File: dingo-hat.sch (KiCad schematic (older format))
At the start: 53 parts, among them J1 LiPo-Power, J10 PJ-037B, J11 Bypass-Power, J12 Chassis-Out, J13 i2c_display, J14 NEOPIXEL, J15 MPU-9250, J2 Raspberry_Pi_2_3, J24 3mm_Mount, J25 3mm_Mount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

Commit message: updated footprints to handsolder
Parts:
- C1: footprint Capacitors_SMD:C_0603 -> Capacitor_SMD:C_0603_1608Metric_Pad1.05x0.95mm_HandSolder
- C3, C9, FB1, FB2, FB3, R1, R10, R11, R12, R13, R14, R2, R3, R4, R5, R6, R7, R8, R9: footprint Resistors_SMD:R_0603 -> Resistor_SMD:R_0603_1608Metric_Pad1.05x0.95mm_HandSolder
- F1, F2: footprint Resistors_SMD:R_1206 -> Resistor_SMD:R_1206_3216Metric_Pad1.42x1.75mm_HandSolder
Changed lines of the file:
@@
 F 0 "R7" H 8820 2896 50  0000 L CNN
 F 1 "10K" H 8820 2805 50  0000 L CNN
-F 2 "Resistors_SMD:R_0603" V 8680 2850 50  0001 C CNN
+F 2 "Resistor_SMD:R_0603_1608Metric_Pad1.05x0.95mm_HandSolder" V 8680 2850 50  0001 C CNN
 F 3 "~" H 8750 2850 50  0001 C CNN
 F 4 "0603" H 0   0   50  0001 C CNN "Package"
@@
 F 0 "R1" V 6200 4900 50  0000 C CNN
 F 1 "470" V 6200 5100 50  0000 C CNN
-F 2 "Resistors_SMD:R_0603" V 6230 5000 50  0001 C CNN
+F 2 "Resistor_SMD:R_0603_1608Metric_Pad1.05x0.95mm_HandSolder" V 6230 5000 50  0001 C CNN
 F 3 "~" H 6300 5000 50  0001 C CNN
 F 4 "0603" H 5000 -1050 50  0001 C CNN "Package"
@@
 F 0 "R3" H 7730 3146 50  0000 R CNN
 F 1 "330" H 7730 3055 50  0000 R CNN
-F 2 "Resistors_SMD:R_0603" V 7730 3100 50  0001 C CNN
+F 2 "Resistor_SMD:R_0603_1608Metric_Pad1.05x0.95mm_HandSolder" V 7730 3100 50  0001 C CNN
 F 3 "~" H 7800 3100 50  0001 C CNN
 F 4 "0603" H 0   0   50  0001 C CNN "Package"
@@
 F 0 "R4" H 7870 3546 50  0000 L CNN
 F 1 "470" H 7870 3455 50  0000 L CNN
-F 2 "Resistors_SMD:R_0603" V 7730 3500 50  0001 C CNN
+F 2 "Resistor_SMD:R_0603_1608Metric_Pad1.05x0.95mm_HandSolder" V 7730 3500 50  0001 C CNN
 F 3 "~" H 7800 3500 50  0001 C CNN
 F 4 "0603" H 0   0   50  0001 C CNN "Package"
@@
 F 0 "R5" H 7730 4646 50  0000 R CNN
 F 1 "330" H 7730 4555 50  0000 R CNN
-F 2 "Resistors_SMD:R_0603" V 7730 4600 50  0001 C CNN
+F 2 "Resistor_SMD:R_0603_1608Metric_Pad1.05x0.95mm_HandSolder" V 7730 4600 50  0001 C CNN
 F 3 "~" H 7800 4600 50  0001 C CNN
 F 4 "0603" H 0   0   50  0001 C CNN "Package"
@@
 F 0 "R6" H 7870 5046 50  0000 L CNN
 F 1 "470" H 7870 4955 50  0000 L CNN
-F 2 "Resistors_SMD:R_0603" V 7730 5000 50  0001 C CNN
+F 2 "Resistor_SMD:R_0603_1608Metric_Pad1.05x0.95mm_HandSolder" V 7730 5000 50  0001 C CNN
 F 3 "~" H 7800 5000 50  0001 C CNN
 F 4 "0603" H 0   0   50  0001 C CNN "Package"
@@
 F 0 "R8" H 3170 1096 50  0000 L CNN
 F 1 "3.9K" H 3170 1005 50  0000 L CNN
-F 2 "Resistors_SMD:R_0603" V 3030 1050 50  0001 C CNN
+F 2 "Resistor_SMD:R_0603_1608Metric_Pad1.05x0.95mm_HandSolder" V 3030 1050 50  0001 C CNN
 F 3 "~" H 3100 1050 50  0001 C CNN
 F 4 "0603" H 3100 1050 50  0001 C CNN "Package"
@@
 F 0 "R9" H 3470 1096 50  0000 L CNN
 F 1 "3.9K" H 3470 1005 50  0000 L CNN
-F 2 "Resistors_SMD:R_0603" V 3330 1050 50  0001 C CNN
+F 2 "Resistor_SMD:R_0603_1608Metric_Pad1.05x0.95mm_HandSolder" V 3330 1050 50  0001 C CNN
 F 3 "~" H 3400 1050 50  0001 C CNN
 F 4 "0603" H 3400 1050 50  0001 C CNN "Package"
@@
 F 0 "R10" H 3770 1096 50  0000 L CNN
 F 1 "3.9K" H 3770 1005 50  0000 L CNN
-F 2 "Resistors_SMD:R_0603" V 3630 1050 50  0001 C CNN
+F 2 "Resistor_SMD:R_0603_1608Metric_Pad1.05x0.95mm_HandSolder" V 3630 1050 50  0001 C CNN
 F 3 "~" H 3700 1050 50  0001 C CNN
 F 4 "0603" H 0   0   50  0001 C CNN "Package"
@@
 F 0 "R11" H 4070 1096 50  0000 L CNN
 F 1 "3.9K" H 4070 1005 50  0000 L CNN
-F 2 "Resistors_SMD:R_0603" V 3930 1050 50  0001 C CNN
+F 2 "Resistor_SMD:R_0603_1608Metric_Pad1.05x0.95mm_HandSolder" V 3930 1050 50  0001 C CNN
 F 3 "~" H 4000 1050 50  0001 C CNN
 F 4 "0603" H 0   0   50  0001 C CNN "Package"
@@
 F 0 "R13" V 4900 6300 50  0000 C CNN
 F 1 "100k" V 4900 6500 50  0000 C CNN
-F 2 "Resistors_SMD:R_0603" V 4930 6400 50  0001 C CNN
+F 2 "Resistor_SMD:R_0603_1608Metric_Pad1.05x0.95mm_HandSolder" V 4930 6400 50  0001 C CNN
 F 3 "~" H 5000 6400 50  0001 C CNN
 F 4 "0603" H 3700 350 50  0001 C CNN "Package"
@@
 F 0 "R12" V 4900 5900 50  0000 C CNN
 F 1 "200k" V 4900 6100 50  0000 C CNN
-F 2 "Resistors_SMD:R_0603" V 4930 6000 50  0001 C CNN
+F 2 "Resistor_SMD:R_0603_1608Metric_Pad1.05x0.95mm_HandSolder" V 4930 6000 50  0001 C CNN
 F 3 "~" H 5000 6000 50  0001 C CNN
 F 4 "0603" H 3700 -50 50  0001 C CNN "Package"
@@
 F 0 "R2" H 2330 6996 50  0000 R CNN
 F 1 "47R" H 2330 6905 50  0000 R CNN
-F 2 "Resistors_SMD:R_0603" V 2330 6950 50  0001 C CNN
+F 2 "Resistor_SMD:R_0603_1608Metric_Pad1.05x0.95mm_HandSolder" V 2330 6950 50  0001 C CNN
 F 3 "~" H 2400 6950 50  0001 C CNN
 F 4 "0603" H -5400 3850 50  0001 C CNN "Package"
@@
 F 0 "C1" H 5415 6446 50  0000 L CNN
 F 1 "DNF" H 5415 6355 50  0000 L CNN
-F 2 "Capacitors_SMD:C_0603" H 5338 6250 50  0001 C CNN
+F 2 "Capacitor_SMD:C_0603_1608Metric_Pad1.05x0.95mm_HandSolder" H 5338 6250 50  0001 C CNN
 F 3 "~" H 5300 6400 50  0001 C CNN
 F 4 "0603" H 5200 6500 50  0000 L TNN "Package"
@@
 F 0 "FB2" V 1450 4300 50  0000 C CNN
 F 1 "Ferrite_Bead_Small" V 1354 4400 50  0001 C CNN
-F 2 "Resistors_SMD:R_0603" V 1430 4400 50  0001 C CNN
+F 2 "Resistor_SMD:R_0603_1608Metric_Pad1.05x0.95mm_HandSolder" V 1430 4400 50  0001 C CNN
 F 3 "~" H 1500 4400 50  0001 C CNN
 F 4 "FERRITE BEAD 8A 22 OHM 0603 1 LN" H 1500 4400 50  0001 C CNN "Description"
@@
 F 0 "FB1" V 1300 5200 50  0000 C CNN
 F 1 "Ferrite_Bead_Small" V 1204 5300 50  0001 C CNN
-F 2 "Resistors_SMD:R_0603" V 1280 5300 50  0001 C CNN
+F 2 "Resistor_SMD:R_0603_1608Metric_Pad1.05x0.95mm_HandSolder" V 1280 5300 50  0001 C CNN
 F 3 "~" H 1350 5300 50  0001 C CNN
 F 4 "FERRITE BEAD 8A 22 OHM 0603 1 LN" H 1350 5300 50  0001 C CNN "Description"
@@
 F 0 "F2" V 3850 4500 50  0000 C TNN
 F 1 "Fuse" V 3662 4600 50  0001 C CNN
-F 2 "Resistors_SMD:R_1206" V 3880 4600 50  0001 C CNN
+F 2 "Resistor_SMD:R_1206_3216Metric_Pad1.42x1.75mm_HandSolder" V 3880 4600 50  0001 C CNN
 F 3 "~" H 3950 4600 50  0001 C CNN
 F 4 "30A" V 3850 4650 50  0000 C TNN "DCR"
@@
 F 0 "F1" V 1050 4300 50  0000 C TNN
 F 1 "Fuse" V 862 4400 50  0001 C CNN
-F 2 "Resistors_SMD:R_1206" V 1080 4400 50  0001 C CNN
+F 2 "Resistor_SMD:R_1206_3216Metric_Pad1.42x1.75mm_HandSolder" V 1080 4400 50  0001 C CNN
 F 3 "~" H 1150 4400 50  0001 C CNN
 F 4 "30A" V 1050 4450 50  0000 C TNN "DCR"
@@
 F 0 "FB3" V 4250 4500 50  0000 C CNN
 F 1 "Ferrite_Bead_Small" V 4154 4600 50  0001 C CNN
-F 2 "Resistors_SMD:R_0603" V 4230 4600 50  0001 C CNN
+F 2 "Resistor_SMD:R_0603_1608Metric_Pad1.05x0.95mm_HandSolder" V 4230 4600 50  0001 C CNN
 F 3 "~" H 4300 4600 50  0001 C CNN
 F 4 "FERRITE BEAD 8A 22 OHM 0603 1 LN" H 4300 4600 50  0001 C CNN "Description"
@@
 F 0 "R14" H 8520 3546 50  0000 L CNN
 F 1 "10K" H 8520 3455 50  0000 L CNN
-F 2 "Resistors_SMD:R_0603" V 8380 3500 50  0001 C CNN
+F 2 "Resistor_SMD:R_0603_1608Metric_Pad1.05x0.95mm_HandSolder" V 8380 3500 50  0001 C CNN
 F 3 "~" H 8450 3500 50  0001 C CNN
 F 4 "0603" H -300 650 50  0001 C CNN "Package"
@@
 F 0 "C9" H 2065 7146 50  0000 L CNN
 F 1 "10uF" H 2065 7055 50  0000 L CNN
-F 2 "Resistors_SMD:R_0603" H 1988 6950 50  0001 C CNN
+F 2 "Resistor_SMD:R_0603_1608Metric_Pad1.05x0.95mm_HandSolder" H 1988 6950 50  0001 C CNN
 F 3 "~" H 1950 7100 50  0001 C CNN
 F 4 "0603" H 1950 7200 50  0000 C TNN "Package"
@@
 F 0 "C3" H 1700 7200 50  0000 L CNN
 F 1 "100nF" H 1700 7000 50  0000 L CNN
-F 2 "Resistors_SMD:R_0603" H 1688 6950 50  0001 C CNN
+F 2 "Resistor_SMD:R_0603_1608Metric_Pad1.05x0.95mm_HandSolder" H 1688 6950 50  0001 C CNN
 F 3 "~" H 1650 7100 50  0001 C CNN
 F 4 "0603" H -1650 -50 50  0001 C CNN "Package"

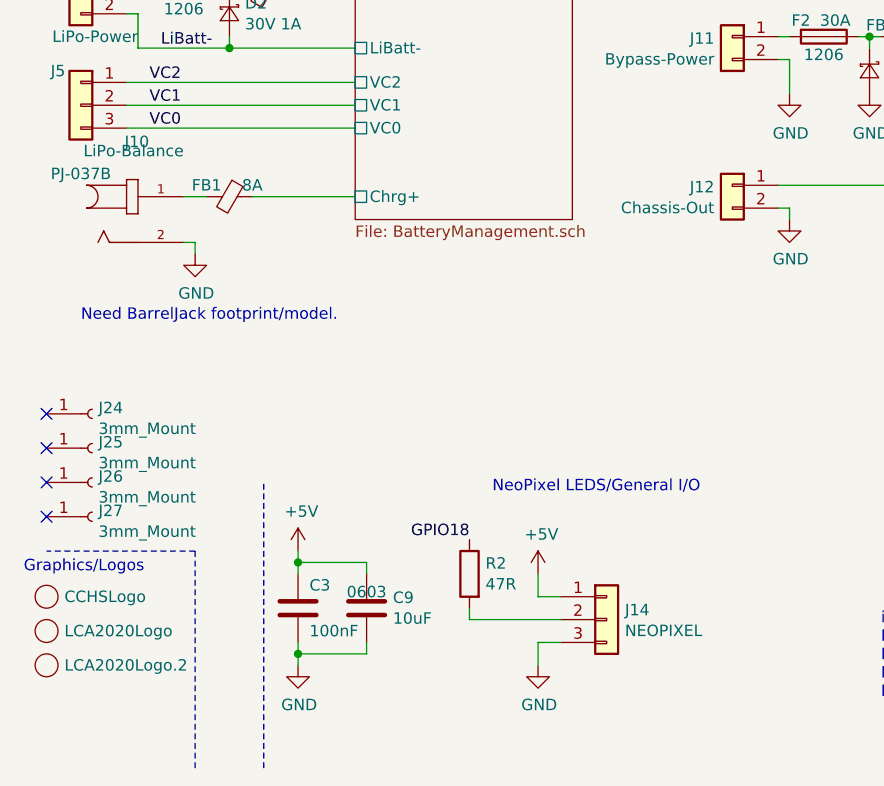
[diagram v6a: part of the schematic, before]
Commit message: Included both oled and MPU on top.  Additional silkscreen designs
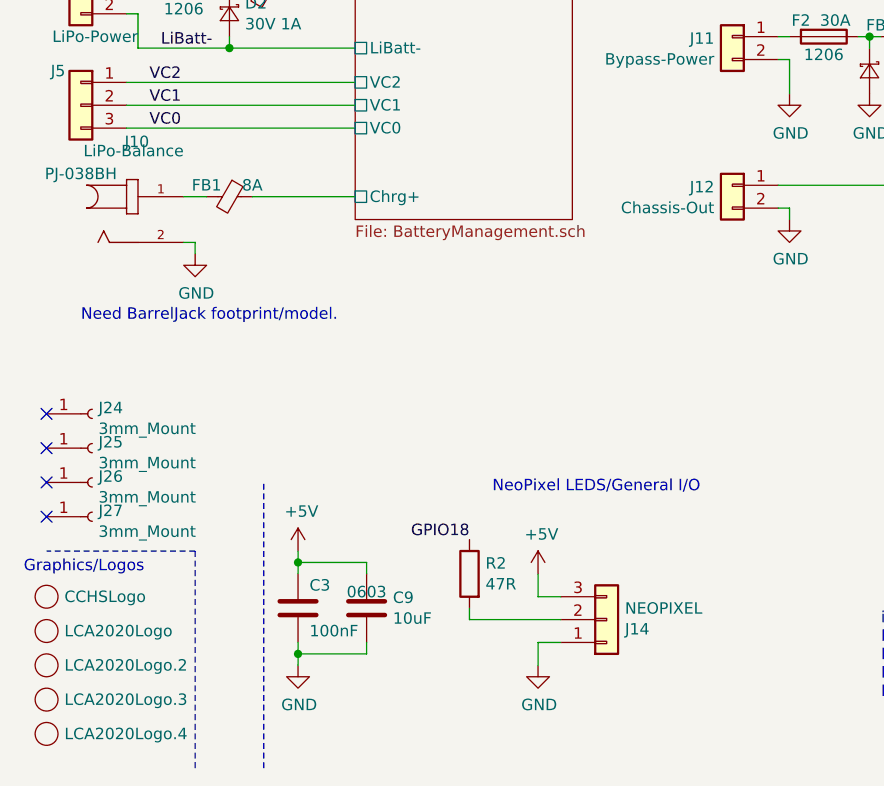
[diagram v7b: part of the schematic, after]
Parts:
- added G4: LCA2020Logo.3, libs:logo-2020.silk, symbol dingo-hat-graphics:LCA2020Logo
- added G5: LCA2020Logo.4, libs:logo-2020.mask, symbol dingo-hat-graphics:LCA2020Logo
- J10: value PJ-037B -> PJ-038BH; footprint libs:CUI_PJ-037B -> libs:CUI_PJ-038BH
- J13: footprint Pin_Headers:Pin_Header_Straight_1x04_Pitch2.54mm -> libs:0.91 OLED
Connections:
- net +5V: now also J14.3 (Pin_3); no longer J14.1 (Pin_1)
- net GND: now also J14.1 (Pin_1); no longer J14.3 (Pin_3)
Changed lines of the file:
@@
 F 3 "~" H 3000 7150 50  0001 C CNN
 	1    3000 7150
-	1    0    0    -1
+	1    0    0    1
 $EndComp
 $Comp
@@
 F 0 "J13" H 6200 3150 50  0000 C CNN
 F 1 "i2c_display" H 6200 2650 50  0000 C CNN
-F 2 "Pin_Headers:Pin_Header_Straight_1x04_Pitch2.54mm" H 6200 2950 50  0001 C CNN
+F 2 "libs:0.91 OLED" H 6200 2950 50  0001 C CNN
 F 3 "~" H 6200 2950 50  0001 C CNN
 F 4 "https://tronixlabs.com.au/sensors/distance/ultrasonic/ultrasonic-distance-sensor-module-hc-sr04-2-450-cm-australia/" H 6200 2950 50  0001 C CNN "Link"
@@
 P 950 5400
 F 0 "J10" H 945 5740 50  0000 C CNN
-F 1 "PJ-037B" H 700 5600 50  0000 C CNN
-F 2 "libs:CUI_PJ-037B" H 950 5400 50  0001 L BNN
+F 1 "PJ-038BH" H 700 5600 50  0000 C CNN
+F 2 "libs:CUI_PJ-038BH" H 950 5400 50  0001 L BNN
 F 3 "https://www.cuidevices.com/product/resource/digikeypdf/pj-037b.pdf" H 950 5400 50  0001 L BNN
 F 4 "2.5A" H 950 5400 50  0001 C CNN "DCR"
@@
 	1    0    0    -1
 $EndComp
+$Comp
+L dingo-hat-graphics:LCA2020Logo G4
+U 1 1 5DDBC2A1
+P 550 7500
+F 0 "G4" H 628 7500 50  0001 L CNN
+F 1 "LCA2020Logo.3" H 628 7500 50  0000 L CNN
+F 2 "libs:logo-2020.silk" H 550 7500 50  0001 C CNN
+F 3 "" H 550 7500 50  0001 C CNN
+	1    550  7500
+	1    0    0    -1
+$EndComp
+$Comp
+L dingo-hat-graphics:LCA2020Logo G5
+U 1 1 5DDBC2AB
+P 550 7650
+F 0 "G5" H 628 7650 50  0001 L CNN
+F 1 "LCA2020Logo.4" H 628 7650 50  0000 L CNN
+F 2 "libs:logo-2020.mask" H 550 7650 50  0001 C CNN
+F 3 "" H 550 7650 50  0001 C CNN
+	1    550  7650
+	1    0    0    -1
+$EndComp

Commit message: Updated silkscreen. Added button
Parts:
- added SW1: GPIO13, Button_Switch_THT:SW_PUSH_6mm, symbol Switch:SW_Push
- J3, J4: footprint Connector_PinSocket_2.54mm:PinSocket_1x04_P2.54mm_Vertical -> Connector_PinHeader_2.54mm:PinHeader_1x04_P2.54mm_Vertical
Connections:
- net +5V: now also J3.4 (Pin_4), J4.4 (Pin_4); no longer J3.1 (Pin_1), J4.1 (Pin_1)
- net GND: now also J3.1 (Pin_1), J4.1 (Pin_1), SW1.2; no longer J3.4 (Pin_4), J4.4 (Pin_4)
- net GPIO13: now also SW1.1
- net GPIO19: now also J4.3 (Pin_3); no longer J4.2 (Pin_2)
- net GPIO26: now also J3.3 (Pin_3); no longer J3.2 (Pin_2)
- net at R5.1: now also J4.2 (Pin_2); no longer J4.3 (Pin_3)
- net at R3.1: now also J3.2 (Pin_2); no longer J3.3 (Pin_3)
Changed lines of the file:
@@
 L Connector_Generic:Conn_01x04 J4
 U 1 1 5C1BDC5B
-P 7300 4350
-F 0 "J4" H 7220 4667 50  0000 C CNN
-F 1 "ULTRA_1" H 7220 4576 50  0000 C CNN
-F 2 "Connector_PinSocket_2.54mm:PinSocket_1x04_P2.54mm_Vertical" H 7300 4350 50  0001 C CNN
-F 3 "~" H 7300 4350 50  0001 C CNN
-F 4 "https://tronixlabs.com.au/sensors/distance/ultrasonic/ultrasonic-distance-sensor-module-hc-sr04-2-450-cm-australia/" H 7300 4350 50  0001 C CNN "Link"
-	1    7300 4350
-	-1   0    0    -1
+P 7300 4450
+F 0 "J4" H 7400 4250 50  0000 C CNN
+F 1 "ULTRA_1" H 7350 4150 50  0000 C CNN
+F 2 "Connector_PinHeader_2.54mm:PinHeader_1x04_P2.54mm_Vertical" H 7300 4450 50  0001 C CNN
+F 3 "~" H 7300 4450 50  0001 C CNN
+F 4 "https://tronixlabs.com.au/sensors/distance/ultrasonic/ultrasonic-distance-sensor-module-hc-sr04-2-450-cm-australia/" H 7300 4450 50  0001 C CNN "Link"
+	1    7300 4450
+	-1   0    0    1
 $EndComp
 $Comp
@@
 L Connector_Generic:Conn_01x04 J3
 U 1 1 5C210D5B
-P 7300 2850
-F 0 "J3" H 7220 3167 50  0000 C CNN
-F 1 "ULTRA_0" H 7220 3076 50  0000 C CNN
-F 2 "Connector_PinSocket_2.54mm:PinSocket_1x04_P2.54mm_Vertical" H 7300 2850 50  0001 C CNN
-F 3 "~" H 7300 2850 50  0001 C CNN
-F 4 "https://tronixlabs.com.au/sensors/distance/ultrasonic/ultrasonic-distance-sensor-module-hc-sr04-2-450-cm-australia/" H 7300 2850 50  0001 C CNN "Link"
-	1    7300 2850
-	-1   0    0    -1
+P 7300 2950
+F 0 "J3" H 7400 2700 50  0000 C CNN
+F 1 "ULTRA_0" H 7350 2600 50  0000 C CNN
+F 2 "Connector_PinHeader_2.54mm:PinHeader_1x04_P2.54mm_Vertical" H 7300 2950 50  0001 C CNN
+F 3 "~" H 7300 2950 50  0001 C CNN
+F 4 "https://tronixlabs.com.au/sensors/distance/ultrasonic/ultrasonic-distance-sensor-module-hc-sr04-2-450-cm-australia/" H 7300 2950 50  0001 C CNN "Link"
+	1    7300 2950
+	-1   0    0    1
 $EndComp
 $Comp
@@
 	1    0    0    -1
 $EndComp
+Text Label 7100 5950 0    50   ~ 0
+GPIO13
+$Comp
+L power:GND #PWR0114
+U 1 1 5DDE8A36
+P 7900 6050
+F 0 "#PWR0114" H 7900 5800 50  0001 C CNN
+F 1 "GND" H 7905 5877 50  0000 C CNN
+F 2 "" H 7900 6050 50  0001 C CNN
+F 3 "" H 7900 6050 50  0001 C CNN
+	1    7900 6050
+	1    0    0    -1
+$EndComp
+Wire Wire Line
+	7800 5950 7900 5950
+Wire Wire Line
+	7900 5950 7900 6050
+Wire Wire Line
+	7400 5950 7100 5950
+$Comp
+L Switch:SW_Push SW1
+U 1 1 5DDE62F1
+P 7600 5950
+F 0 "SW1" H 7600 6235 50  0000 C CNN
+F 1 "GPIO13" H 7600 6144 50  0000 C CNN
+F 2 "Button_Switch_THT:SW_PUSH_6mm" H 7600 6150 50  0001 C CNN
+F 3 "~" H 7600 6150 50  0001 C CNN
+	1    7600 5950
+	1    0    0    -1
+$EndComp
